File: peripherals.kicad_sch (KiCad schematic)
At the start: 5 parts, among them J1 Micro_SD_Card, J6 Conn_01x04_Socket

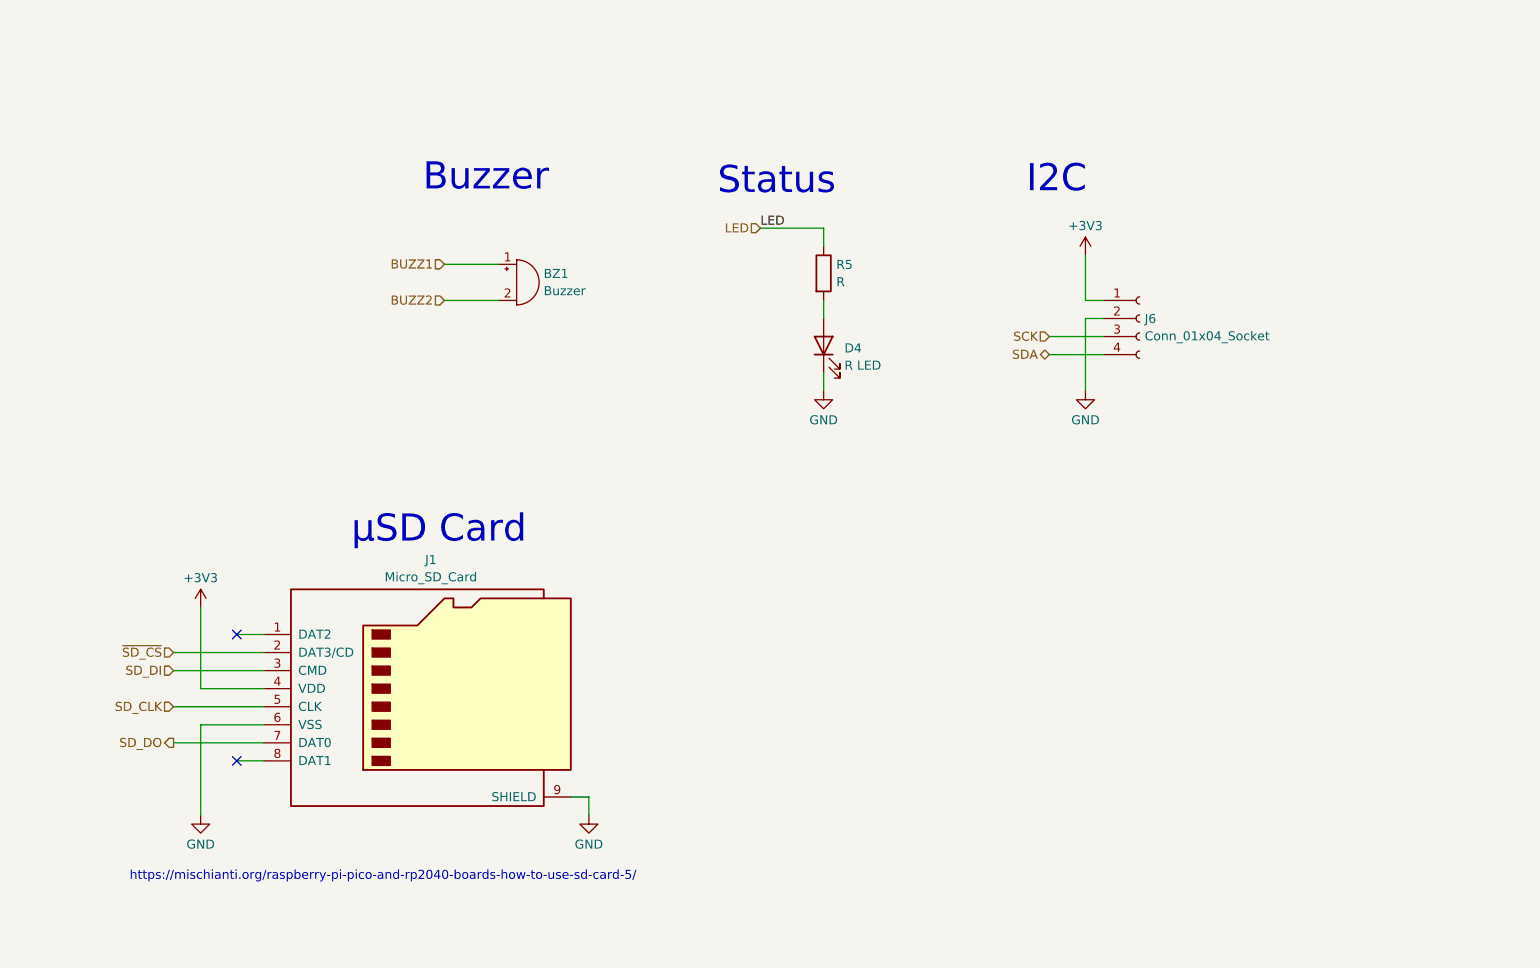
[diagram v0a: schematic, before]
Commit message: Further work, most components now present
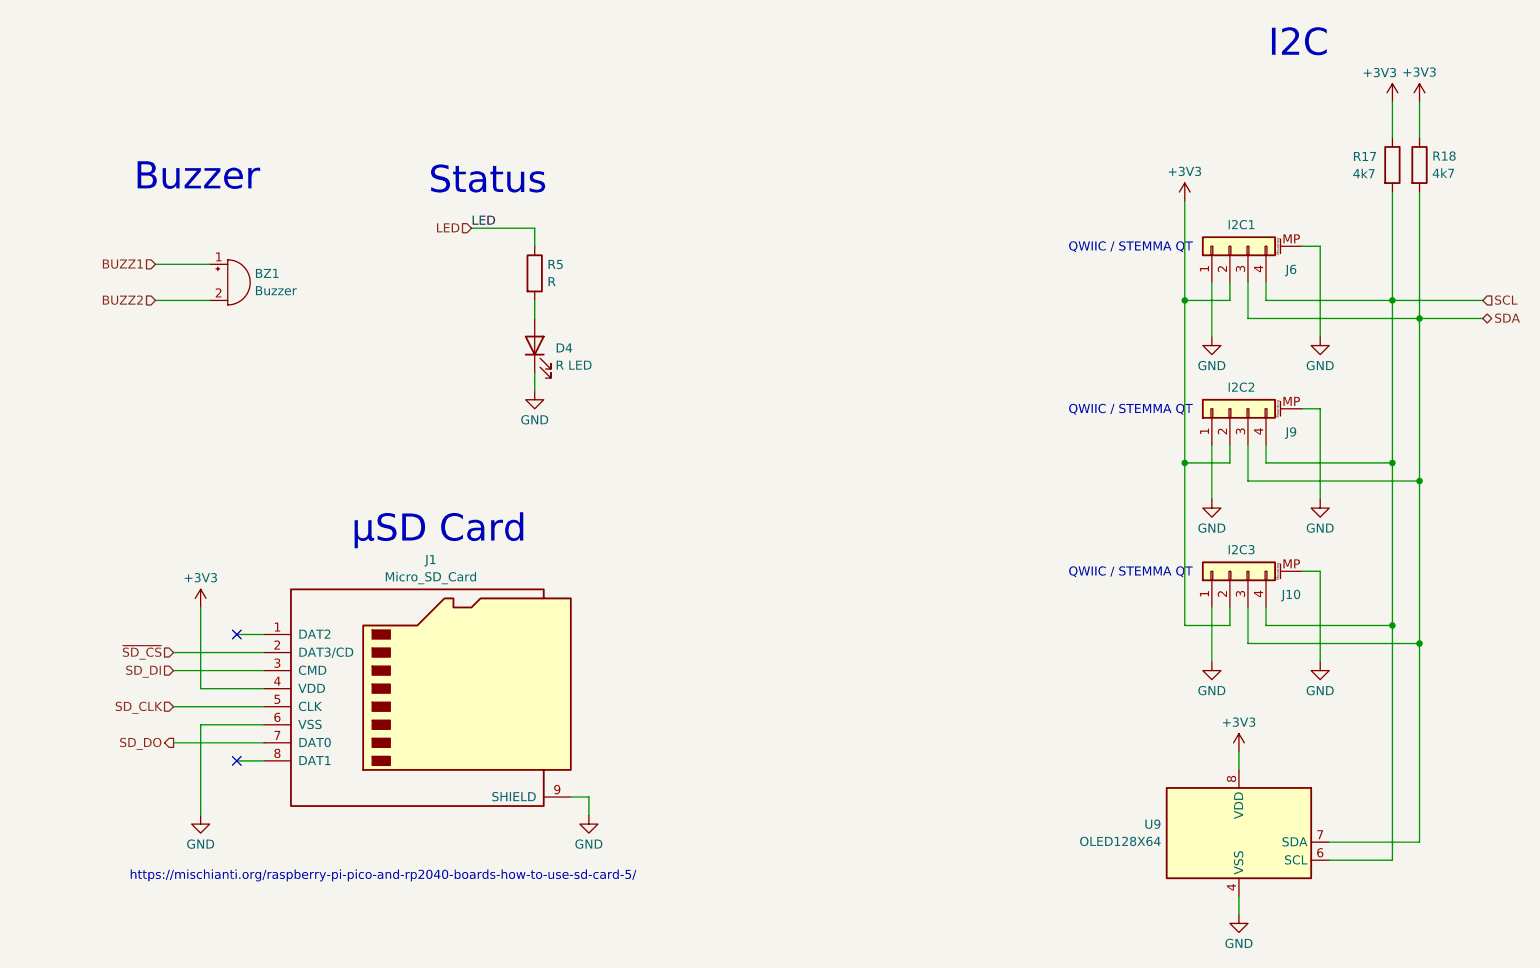
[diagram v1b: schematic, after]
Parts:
- removed J6: Conn_01x04_Socket, symbol Connector:Conn_01x04_Socket
- added J10: I2C3, Connector_JST:JST_SH_SM04B-SRSS-TB_1x04-1MP_P1.00mm_Horizontal, symbol Connector_Generic_MountingPin:Conn_01x04_MountingPin
- added J6: I2C1, Connector_JST:JST_SH_SM04B-SRSS-TB_1x04-1MP_P1.00mm_Horizontal, symbol Connector_Generic_MountingPin:Conn_01x04_MountingPin
- added J9: I2C2, Connector_JST:JST_SH_SM04B-SRSS-TB_1x04-1MP_P1.00mm_Horizontal, symbol Connector_Generic_MountingPin:Conn_01x04_MountingPin
- added R17, R18: 4k7, symbol Device:R
- added U9: OLED128X64, symbol local:OLED128X64
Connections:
- net +3V3: now also J10.2 (Pin_2), J6.2 (Pin_2), J9.2 (Pin_2), R17.1, R18.1, U9.8 (VDD)
- net GND: now also J10.1 (Pin_1), J10.MP (MountPin), J6.1 (Pin_1), J6.MP (MountPin), J9.1 (Pin_1), J9.MP (MountPin), U9.4 (VSS)
- net SDA: now also J10.3 (Pin_3), J6.3 (Pin_3), J9.3 (Pin_3), R18.2, U9.7 (SDA)
- new net SCL: J10.4 (Pin_4), J6.4 (Pin_4), J9.4 (Pin_4), R17.2, U9.6 (SCL)
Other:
- note added: "QWIIC / STEMMA QT"
- moved on the sheet: BZ1, D4, R5
